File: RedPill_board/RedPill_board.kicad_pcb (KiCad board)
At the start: 2 copper layers, 25.4 x 62.2 mm, 60 parts, among them J1 PROG, J2 USB_C_Receptacle_USB2.0, J3 Conn_01x22, J4 Conn_01x22, Q1 S9013, SW1 RESET, U1 FCM32F103CBT6, U2 ME6211C33M5G-N, U3 STM32F401RCT6, Y1 8MHz, Y2 8MHz

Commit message: Minor modifications
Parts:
- removed C18: 100n, Capacitor_SMD:C_0603_1608Metric
- removed JP1: SB60, Jumper:SolderJumper-2_P1.3mm_Open_RoundedPad1.0x1.5mm
- added R26: 100k, Resistor_SMD:R_0603_1608Metric, F.Cu at (133.5, 95.4)
- J1: footprint Connector_PinHeader_2.54mm:PinHeader_1x04_P2.54mm_Vertical -> Connector_PinHeader_1.27mm:PinHeader_1x04_P1.27mm_Vertical
- Y1: footprint Crystal:Crystal_HC49-4H_Vertical -> Crystal:Crystal_SMD_3225-4Pin_3.2x2.5mm
- moved J1 5.57 mm to (101.6, 62.0)
- moved Y1 2.27 mm to (112.2, 86.0)
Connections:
- net VDDA renamed Net-(U3-VREF+)
- U3 pad 12: GNDA -> GND

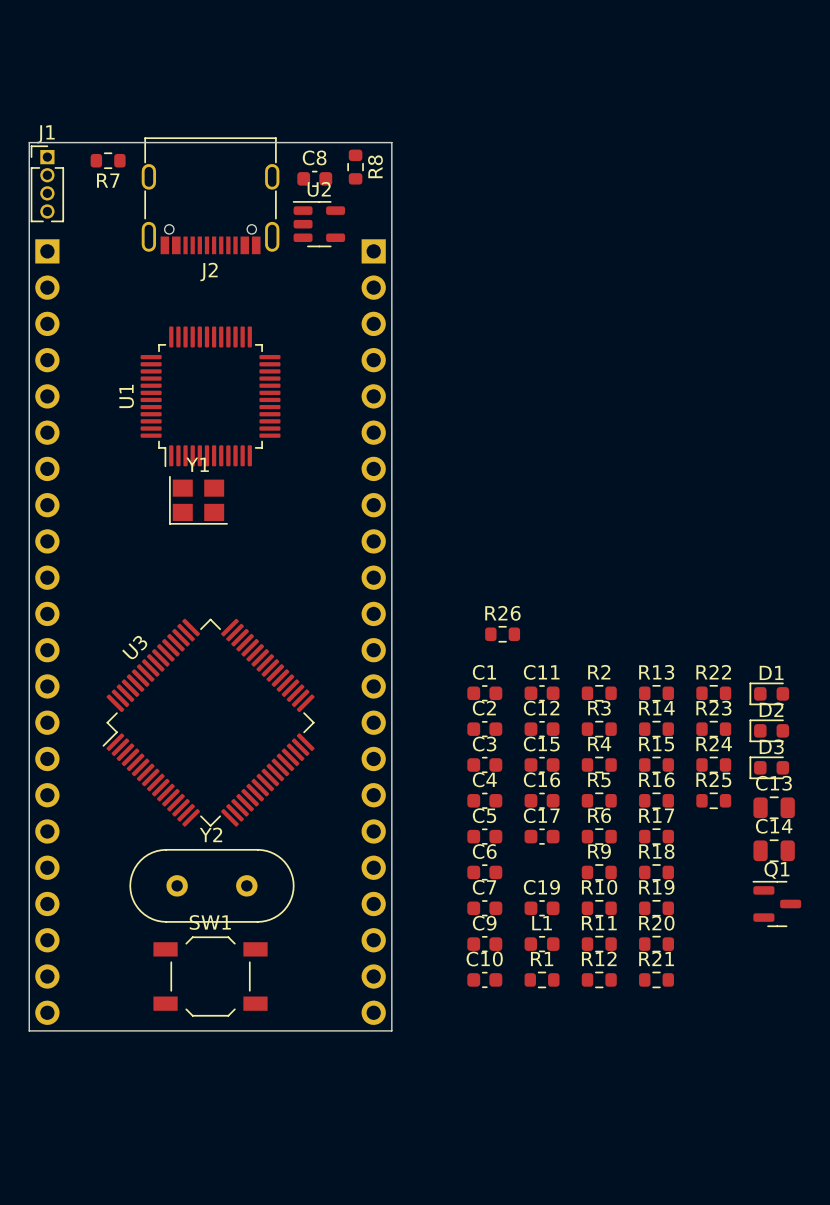
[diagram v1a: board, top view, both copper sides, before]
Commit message: Fit parts on top side
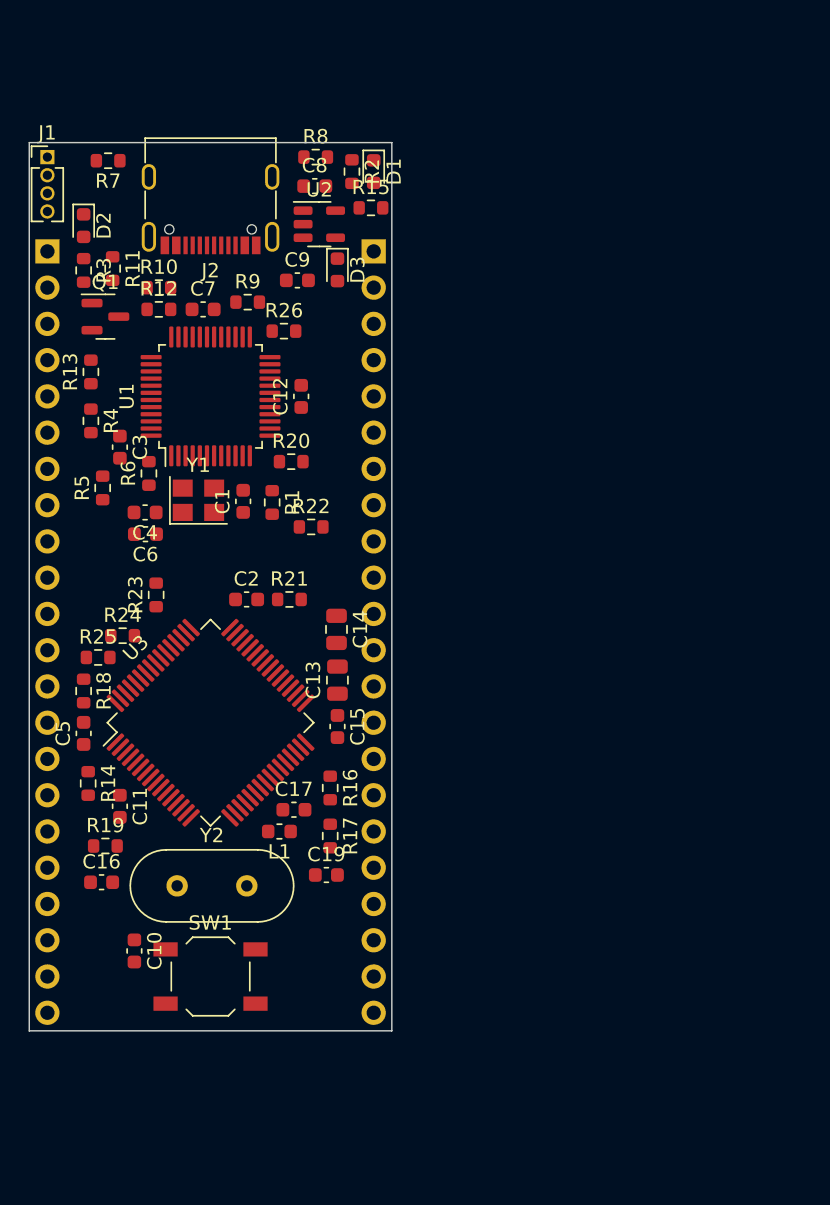
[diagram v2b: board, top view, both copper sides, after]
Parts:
- moved Q1 62.5 mm to (105.7, 73.2)
- moved D2 59.8 mm to (104.1, 66.8), turned to -90 degrees
- moved R11 58.3 mm to (106.2, 69.8), turned to -90 degrees
- moved R12 56.2 mm to (109.4, 72.6)
- moved R10 53.3 mm to (109.4, 71.1)
- moved R3 48.3 mm to (104.1, 69.9), turned to -90 degrees
- moved C9 48.3 mm to (119.1, 70.6)
- moved R9 46.9 mm to (115.6, 72.1)
- moved C7 46.4 mm to (112.5, 72.6)
- moved D3 46.3 mm to (121.9, 69.9), turned to -90 degrees
- moved D1 46.0 mm to (124.5, 63.0), turned to -90 degrees
- moved R13 45.6 mm to (104.6, 77.0), turned to 90 degrees
- moved R25 44.3 mm to (105.2, 97.0)
- moved R15 43.9 mm to (124.3, 65.5)
- moved R4 43.0 mm to (104.6, 80.5), turned to -90 degrees
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
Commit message: Routing in progress.
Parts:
- added C18: 100n, Capacitor_SMD:C_0603_1608Metric, F.Cu at (116.6, 109.0)
- added F1: 1A, Fuse:Fuse_1206_3216Metric, F.Cu at (120.9, 56.1)
- added R27: 22, Resistor_SMD:R_0603_1608Metric, F.Cu at (120.1, 86.4)
- C14: footprint Capacitor_SMD:C_0805_2012Metric -> Capacitor_SMD:C_0603_1608Metric
- J3, J4: value Conn_01x22 -> Conn_01x26; footprint Connector_PinHeader_2.54mm:PinHeader_1x22_P2.54mm_Vertical -> Connector_PinHeader_2.54mm:PinHeader_1x26_P2.54mm_Vertical
- R15, R2, R3: value 100 -> 220
- R26: value 100k -> 10k
- U1: value FCM32F103CBT6 -> STM32F103CBTx
- U2: value ME6211C33M5G-N -> AMS1117-3.3; footprint Package_TO_SOT_SMD:SOT-23-5 -> Package_TO_SOT_SMD:SOT-223-3_TabPin2
- moved R26 35.1 mm to (104.4, 106.4), turned to -90 degrees
- moved R17 32.3 mm to (120.4, 77.2), turned to 0 degrees
- moved C12 31.4 mm to (109.2, 108.5), turned to -45 degrees
- moved R16 27.2 mm to (120.4, 79.0), turned to 180 degrees
- moved C5 26.9 mm to (115.1, 77.7), turned to 180 degrees
- moved R19 25.6 mm to (114.8, 86.4), turned to -90 degrees
- moved C2 24.7 mm to (119.4, 68.6), turned to -90 degrees
- moved D1 20.8 mm to (103.9, 60.2), turned to 180 degrees
- moved R14 19.8 mm to (107.7, 86.4)
- moved C19 19.6 mm to (104.6, 101.6), turned to 90 degrees
- moved R8 18.0 mm to (103.9, 54.9), turned to 180 degrees
- moved R15 17.5 mm to (128.5, 82.5), turned to 90 degrees
- moved R2 17.0 mm to (105.9, 62.0), turned to 180 degrees
- moved D3 17.0 mm to (129.0, 85.3), turned to 180 degrees
- moved C11 15.5 mm to (120.1, 115.1)
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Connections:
- C12 pad 1: /T_NRST -> GND
- C12 pad 2: GND -> Net-(U3-VREF+)
- J2 pad A4: +5V -> Net-(F1-Pad1)
- J2 pad A9: +5V -> Net-(F1-Pad1)
- J2 pad B4: +5V -> Net-(F1-Pad1)
- J2 pad B9: +5V -> Net-(F1-Pad1)
- J3 pad 1: unconnected-(J3-Pin_1-Pad1) -> +3V3
- J3 pad 10: unconnected-(J3-Pin_10-Pad10) -> /PB6
- J3 pad 11: unconnected-(J3-Pin_11-Pad11) -> /PB7
- J3 pad 12: unconnected-(J3-Pin_12-Pad12) -> /PB8
- J3 pad 13: unconnected-(J3-Pin_13-Pad13) -> /PB9
- J3 pad 14: unconnected-(J3-Pin_14-Pad14) -> GND
- J3 pad 15: unconnected-(J3-Pin_15-Pad15) -> /PC13
- J3 pad 16: unconnected-(J3-Pin_16-Pad16) -> /PC14
- J3 pad 17: unconnected-(J3-Pin_17-Pad17) -> /PC15
- J3 pad 18: unconnected-(J3-Pin_18-Pad18) -> /PC0
- J3 pad 19: unconnected-(J3-Pin_19-Pad19) -> /PC1
- J3 pad 2: unconnected-(J3-Pin_2-Pad2) -> /PA15
- J3 pad 20: unconnected-(J3-Pin_20-Pad20) -> /PC2
- J3 pad 21: unconnected-(J3-Pin_21-Pad21) -> /PC3
- J3 pad 22: unconnected-(J3-Pin_22-Pad22) -> /PA0
- J3 pad 3: unconnected-(J3-Pin_3-Pad3) -> /PC10
- J3 pad 4: unconnected-(J3-Pin_4-Pad4) -> /PC11
- J3 pad 5: unconnected-(J3-Pin_5-Pad5) -> /PC12
- J3 pad 6: unconnected-(J3-Pin_6-Pad6) -> /PD2
- J3 pad 7: unconnected-(J3-Pin_7-Pad7) -> /PB3
- J3 pad 8: unconnected-(J3-Pin_8-Pad8) -> /PB4
- J3 pad 9: unconnected-(J3-Pin_9-Pad9) -> /PB5
- J4 pad 1: unconnected-(J4-Pin_1-Pad1) -> +5V
- J4 pad 10: unconnected-(J4-Pin_10-Pad10) -> /PC7
- J4 pad 11: unconnected-(J4-Pin_11-Pad11) -> /PC6
- J4 pad 12: unconnected-(J4-Pin_12-Pad12) -> /PB15
- J4 pad 13: unconnected-(J4-Pin_13-Pad13) -> /PB14
- J4 pad 14: unconnected-(J4-Pin_14-Pad14) -> /PB13
- J4 pad 15: unconnected-(J4-Pin_15-Pad15) -> /PB12
- J4 pad 16: unconnected-(J4-Pin_16-Pad16) -> /PB10
- J4 pad 17: unconnected-(J4-Pin_17-Pad17) -> /PB2
- J4 pad 18: unconnected-(J4-Pin_18-Pad18) -> /PB1
- J4 pad 19: unconnected-(J4-Pin_19-Pad19) -> /PB0
- J4 pad 2: unconnected-(J4-Pin_2-Pad2) -> +3V3
- J4 pad 20: unconnected-(J4-Pin_20-Pad20) -> /PC5
- J4 pad 21: unconnected-(J4-Pin_21-Pad21) -> /PC4
- J4 pad 22: unconnected-(J4-Pin_22-Pad22) -> /PA7
- J4 pad 3: unconnected-(J4-Pin_3-Pad3) -> /PA12
- J4 pad 4: unconnected-(J4-Pin_4-Pad4) -> /PA11
- J4 pad 5: unconnected-(J4-Pin_5-Pad5) -> /PA10
- J4 pad 6: unconnected-(J4-Pin_6-Pad6) -> /PA9
- J4 pad 7: unconnected-(J4-Pin_7-Pad7) -> /PA8
- J4 pad 8: unconnected-(J4-Pin_8-Pad8) -> /PC9
- J4 pad 9: unconnected-(J4-Pin_9-Pad9) -> /PC8
- R19 pad 2: /USART_TX -> /PA2
- R20 pad 2: /USART_RX -> /PA3
- R23 pad 1: Net-(U3-PA15) -> /PA15
- R24 pad 2: Net-(U3-PB3) -> /PB3
- R25 pad 2: Net-(U3-PB4) -> /PB4
- R26 pad 2: /T_NRST -> Net-(U3-NRST)
- SW1 pad 1: /T_NRST -> Net-(U3-NRST)
- U1 pad 1: unconnected-(U1-NC-Pad1) -> +3V3
- U2 pad 1: +5V -> GND
- U2 pad 2: GND -> +3V3
- U3 pad 10: unconnected-(U3-PC2-Pad10) -> /PC2
- U3 pad 11: unconnected-(U3-PC3-Pad11) -> /PC3
- U3 pad 14: unconnected-(U3-PA0-Pad14) -> /PA0
- U3 pad 15: unconnected-(U3-PA1-Pad15) -> /PA1
- U3 pad 16: /USART_TX -> /PA2
- U3 pad 17: /USART_RX -> /PA3
- U3 pad 2: unconnected-(U3-PC13-Pad2) -> /PC13
- U3 pad 20: unconnected-(U3-PA4-Pad20) -> /PA4
- U3 pad 21: unconnected-(U3-PA5-Pad21) -> /PA5
- U3 pad 22: unconnected-(U3-PA6-Pad22) -> /PA6
- U3 pad 23: unconnected-(U3-PA7-Pad23) -> /PA7
- U3 pad 24: unconnected-(U3-PC4-Pad24) -> /PC4
- U3 pad 25: unconnected-(U3-PC5-Pad25) -> /PC5
- U3 pad 26: unconnected-(U3-PB0-Pad26) -> /PB0
- U3 pad 27: unconnected-(U3-PB1-Pad27) -> /PB1
- U3 pad 28: unconnected-(U3-PB2-Pad28) -> /PB2
- U3 pad 29: unconnected-(U3-PB10-Pad29) -> /PB10
- U3 pad 3: unconnected-(U3-PC14-Pad3) -> /PC14
- U3 pad 33: unconnected-(U3-PB12-Pad33) -> /PB12
- U3 pad 34: unconnected-(U3-PB13-Pad34) -> /PB13
- U3 pad 35: unconnected-(U3-PB14-Pad35) -> /PB14
- U3 pad 36: unconnected-(U3-PB15-Pad36) -> /PB15
- U3 pad 37: unconnected-(U3-PC6-Pad37) -> /PC6
- U3 pad 38: unconnected-(U3-PC7-Pad38) -> /PC7
- U3 pad 39: unconnected-(U3-PC8-Pad39) -> /PC8
- U3 pad 4: unconnected-(U3-PC15-Pad4) -> /PC15
- U3 pad 40: unconnected-(U3-PC9-Pad40) -> /PC9
- U3 pad 41: unconnected-(U3-PA8-Pad41) -> /PA8
- U3 pad 42: unconnected-(U3-PA9-Pad42) -> /PA9
- U3 pad 43: unconnected-(U3-PA10-Pad43) -> /PA10
- U3 pad 44: unconnected-(U3-PA11-Pad44) -> /PA11
- U3 pad 45: unconnected-(U3-PA12-Pad45) -> /PA12
- U3 pad 50: Net-(U3-PA15) -> /PA15
- U3 pad 51: unconnected-(U3-PC10-Pad51) -> /PC10
- U3 pad 52: unconnected-(U3-PC11-Pad52) -> /PC11
- U3 pad 53: unconnected-(U3-PC12-Pad53) -> /PC12
- U3 pad 54: unconnected-(U3-PD2-Pad54) -> /PD2
- U3 pad 55: Net-(U3-PB3) -> /PB3
- U3 pad 56: Net-(U3-PB4) -> /PB4
- U3 pad 57: unconnected-(U3-PB5-Pad57) -> /PB5
- U3 pad 58: unconnected-(U3-PB6-Pad58) -> /PB6
- U3 pad 59: unconnected-(U3-PB7-Pad59) -> /PB7
- U3 pad 61: unconnected-(U3-PB8-Pad61) -> /PB8
- U3 pad 62: unconnected-(U3-PB9-Pad62) -> /PB9
- U3 pad 7: /T_NRST -> Net-(U3-NRST)
- U3 pad 8: unconnected-(U3-PC0-Pad8) -> /PC0
- U3 pad 9: unconnected-(U3-PC1-Pad9) -> /PC1
- Y1 pad 2: /PGM_OSC_OUT -> GND
- Y1 pad 3: (no net) -> /PGM_OSC_OUT
- Y1 pad 4: (no net) -> GND
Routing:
- net +3V3: track 0.00 -> 183.1 mm, vias 0 -> 2
- net GND: track 0.00 -> 100.3 mm, vias 0 -> 93
- net +5V: track 0.00 -> 50.6 mm, vias 0 -> 5
- net /MCO: track 0.00 -> 36.1 mm, vias 0 -> 2
- net Net-(U3-NRST): track 0.00 -> 30.2 mm
- net /T_JTDO_SWO: track 0.00 -> 29.3 mm, vias 0 -> 2
- net /T_JTCK_SWCLK: track 0.00 -> 26.1 mm, vias 0 -> 3
- net /T_JTMS_SWDIO: track 0.00 -> 24.8 mm, vias 0 -> 2
- net /PA15: track 0.00 -> 22.7 mm, vias 0 -> 1
- net Net-(U1-PA8): track 0.00 -> 21.8 mm, vias 0 -> 2
- net Net-(U3-PH1): track 0.00 -> 20.6 mm
- net /T_NRST: track 0.00 -> 18.8 mm, vias 0 -> 2
- net /T_JRST: track 0.00 -> 18.7 mm, vias 0 -> 2
- net /PB3: track 0.00 -> 17.1 mm, vias 0 -> 2
- net /T_JTDI: track 0.00 -> 16.9 mm, vias 0 -> 2
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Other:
- board size 25.4 x 62.2 mm -> 25.4 x 80.2 mm

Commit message: Routed.
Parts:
- moved D3 9.77 mm to (119.5, 83.2), turned to 0 degrees
- moved R15 9.09 mm to (119.5, 81.4), turned to 180 degrees
- moved C17 1.14 mm to (115.3, 93.0)
- moved C14 0.92 mm to (121.7, 91.4), turned to 90 degrees
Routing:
- net /PA3: track 0.00 -> 49.6 mm, vias 0 -> 2
- net /PA2: track 0.00 -> 46.9 mm, vias 0 -> 2
- net /PA6: track 0.00 -> 32.1 mm, vias 0 -> 1
- net /PA4: track 0.00 -> 30.9 mm, vias 0 -> 1
- net Net-(U3-NRST): track 30.2 -> 60.9 mm, vias 0 -> 3
- net /PA5: track 0.00 -> 29.9 mm, vias 0 -> 1
- net /PC10: track 0.00 -> 29.4 mm, vias 0 -> 1
- net /PC11: track 0.00 -> 26.6 mm, vias 0 -> 1
- net /PA12: track 0.00 -> 26.3 mm, vias 0 -> 1
- net /PC4: track 0.00 -> 24.4 mm, vias 0 -> 1
- net /PA11: track 0.00 -> 24.1 mm, vias 0 -> 1
- net /PA1: track 0.00 -> 23.6 mm, vias 0 -> 1
- net /PB4: track 0.00 -> 22.5 mm, vias 0 -> 2
- net /PA0: track 0.00 -> 22.5 mm, vias 0 -> 1
- net /PA10: track 0.00 -> 21.8 mm, vias 0 -> 1
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- added copper zone on B.Cu, net GND
- added copper zone on F.Cu, net GND
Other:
- board text added: "LOST THE GAME"

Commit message: Added texts and logo.
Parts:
- added G***: LOGO, lib:semlogo, F.Cu at (113.0, 122.0)
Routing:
- net GND: track 120.8 -> 130.2 mm, vias 110 -> 140
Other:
- board text added: "+3.3V"
- board text added: "+5V"
- board text added: "Based and redpilled STM32F401 board"
- board text added: "Committed by W.P & H.K."
- board text added: "DID IT TAKE LONG TO DESOLDER?"
- board text added: "GND"
- board text added: "PA0"
- board text added: "PA1"
- board text added: "PA10"
- board text added: "PA11"
- board text added: "PA12"
- board text added: "PA15"
- board text added: "PA2"
- board text added: "PA3"
- board text added: "PA4"
- board text added: "PA5"
- board text added: "PA6"
- board text added: "PA7"
- board text added: "PA8"
- board text added: "PA9"
- board text added: "PB0"
- board text added: "PB1"
- board text added: "PB10"
- board text added: "PB12"
- board text added: "PB13"
- board text added: "PB14"
- board text added: "PB15"
- board text added: "PB2"
- board text added: "PB3"
- board text added: "PB4"
- board text added: "PB5"
- board text added: "PB6"
- board text added: "PB7"
- board text added: "PB8"
- board text added: "PB9"
- board text added: "PC0"
- board text added: "PC1"
- board text added: "PC10"
- board text added: "PC11"
- board text added: "PC12"
- board text added: "PC13"
- board text added: "PC14"
- board text added: "PC15"
- board text added: "PC2"
- board text added: "PC3"
- board text added: "PC4"
- board text added: "PC5"
- board text added: "PC6"
- board text added: "PC7"
- board text added: "PC8"
- board text added: "PC9"
- board text added: "PD2"
- board text added: "Rev.A"
- board text added: "SWD on PA13,PA14"
- board text added: "UART on PA2,PA3"
- board text added: "Y THO"

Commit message: Reviewed.
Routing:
- net GND: track 130.2 -> 128.9 mm, vias 140 -> 139
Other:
- board text added: "+3V3"
- board text removed: "+3.3V"

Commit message: Sent to fab.
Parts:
- C13: value 2u2 -> 4.7uF
- Y1: footprint Crystal:Crystal_SMD_3225-4Pin_3.2x2.5mm -> Crystal:Crystal_SMD_5032-2Pin_5.0x3.2mm
- moved C6 1.02 mm to (116.6, 80.8)
- moved R5 0.64 mm to (104.5, 80.8)
- moved C4 0.51 mm to (108.5, 80.8)
- moved R6 0.51 mm to (106.4, 80.8)
- moved Y1 0.25 mm to (112.5, 80.5)
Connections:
- Y1 pad 2: GND -> /PGM_OSC_OUT
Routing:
- net GND: track 128.9 -> 125.2 mm
- net /PGM_OSC_OUT: track 7.11 -> 9.41 mm
- net Net-(U1-PC13): track 8.30 -> 8.93 mm

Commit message: Revision A1 + UART test firmware.
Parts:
- SW1: moved to B.Cu
- moved G*** 1.91 mm to (113.0, 124.0)
- turned SW1 to 180 degrees
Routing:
- net Net-(U3-NRST): vias 3 -> 4
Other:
- board text added: "Rev.A1"
- board text removed: "Rev.A"
